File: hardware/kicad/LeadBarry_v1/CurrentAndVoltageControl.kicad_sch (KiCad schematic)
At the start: 37 parts, among them J1 Screw_Terminal_01x02, J2 Screw_Terminal_01x02, J3 Screw_Terminal_01x02, J4 Screw_Terminal_01x02, Q1 SS9014, U2 INA3221_Module, U3 LM2596S_Module

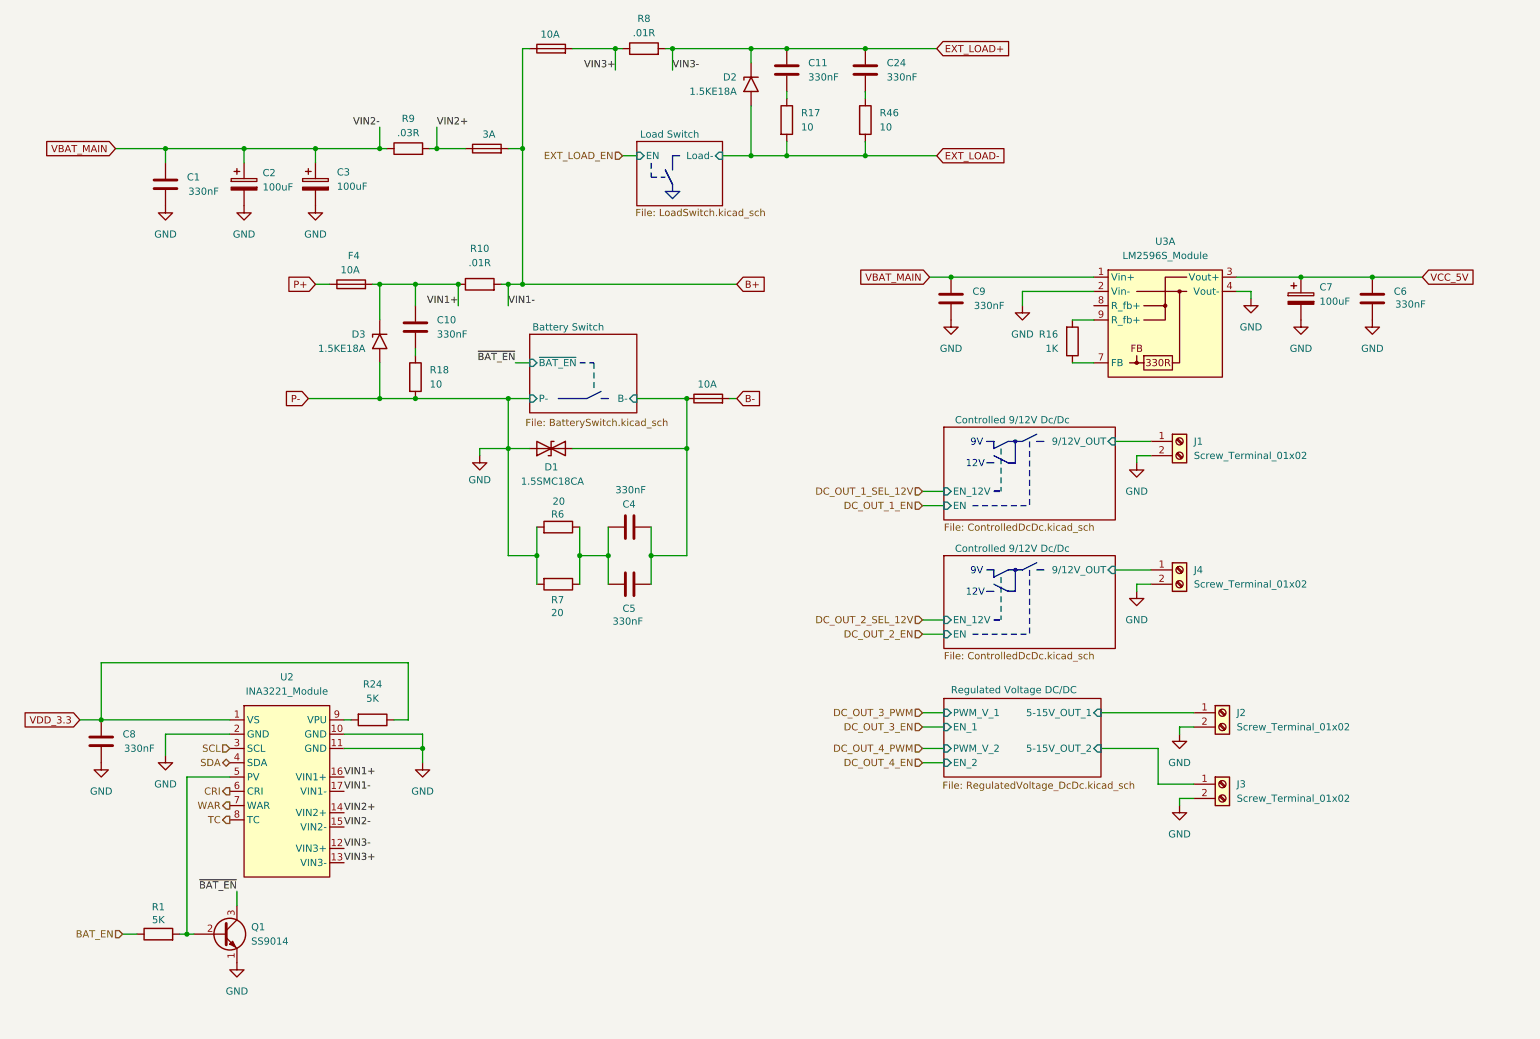
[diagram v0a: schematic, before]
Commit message: fix: PoE sockets and DC output status leds were added
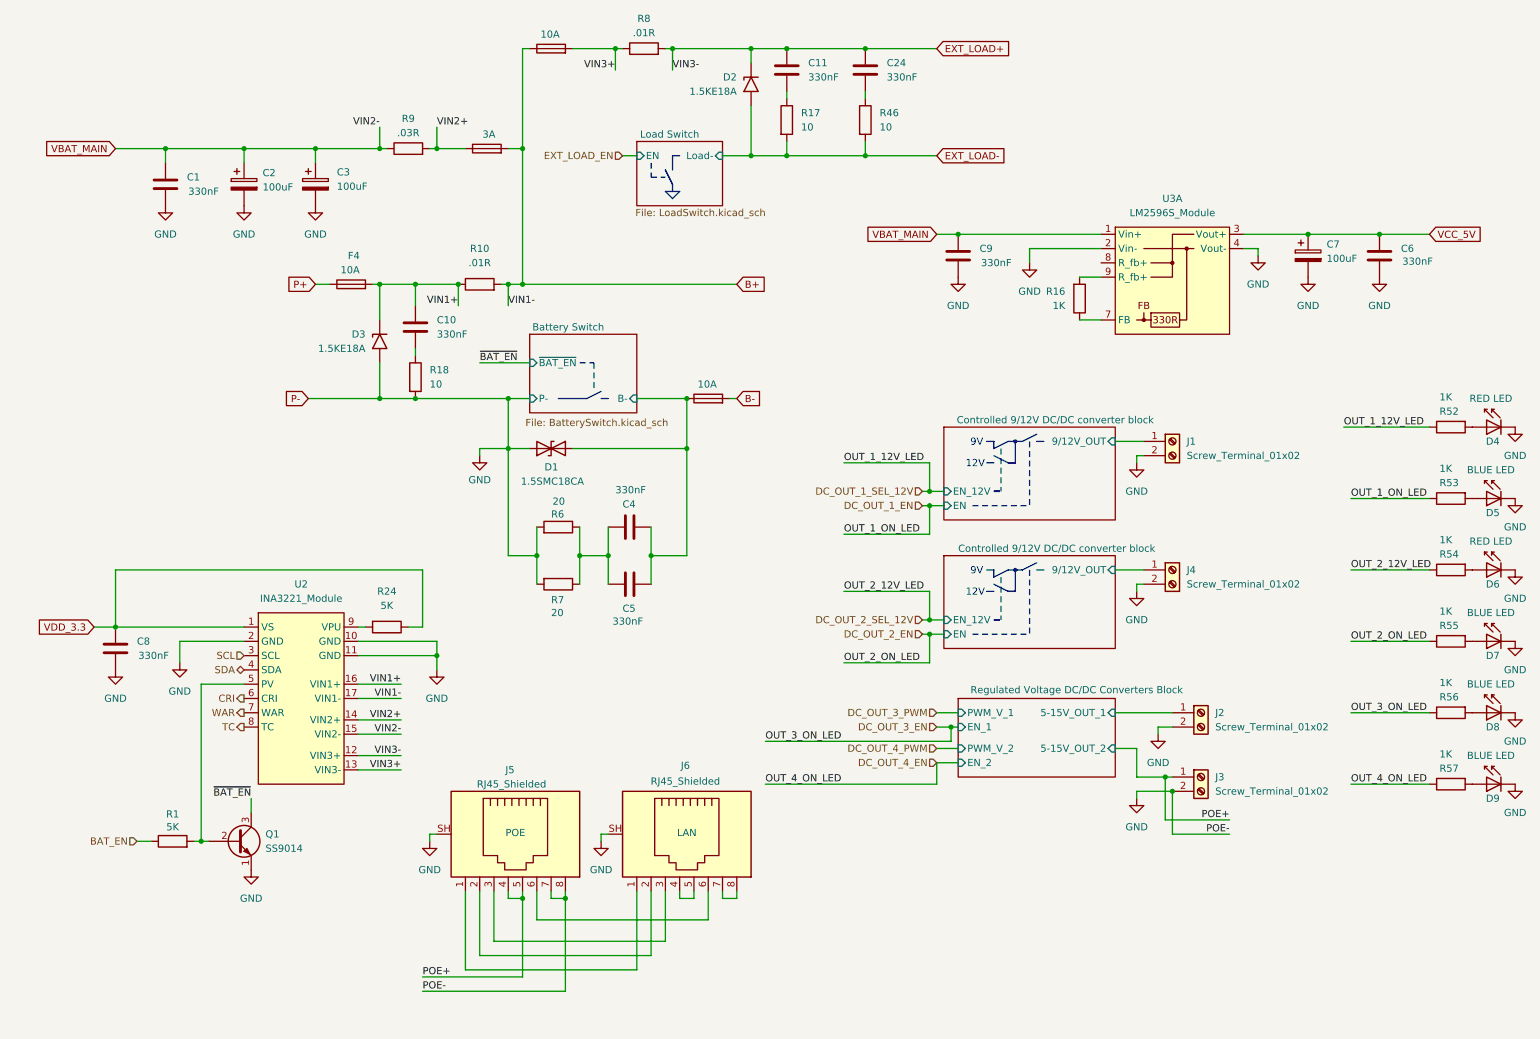
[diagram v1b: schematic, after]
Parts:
- added D4, D5, D6, D7, D8, D9: CQY99, LED_SMD:LED_1206_3216Metric_Pad1.42x1.75mm_HandSolder, symbol LED:CQY99
- added J5, J6: RJ45_Shielded, Connector_RJ:RJ45_Ninigi_GE, symbol Connector:RJ45_Shielded
- added R52, R53, R54, R55, R56, R57: 1K, Resistor_SMD:R_0805_2012Metric_Pad1.20x1.40mm_HandSolder, symbol Device:R
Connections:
- net DC_OUT_1_EN: now also R53.1
- net DC_OUT_1_SEL_12V: now also R52.1
- net DC_OUT_2_EN: now also R55.1
- net DC_OUT_2_SEL_12V: now also R54.1
- net DC_OUT_3_EN: now also R56.1
- net DC_OUT_4_EN: now also R57.1
- net GND: now also D4.1 (K), D5.1 (K), D6.1 (K), D7.1 (K), D8.1 (K), D9.1 (K), J5.7, J5.8, J5.SH, J6.SH
- net Regulated Voltage DC DC/5-15V_OUT_2 renamed POE+
- net POE+: now also J5.4, J5.5
- new net: D4.2 (A), R52.2
- new net: D9.2 (A), R57.2
- new net: D6.2 (A), R54.2
- new net: J5.1, J6.1
- new net: J5.2, J6.2
- new net: J5.3, J6.3
- new net: J6.4, J6.5
- new net: J5.6, J6.6
- new net: J6.7, J6.8
- new net: D8.2 (A), R56.2
- new net: D7.2 (A), R55.2
- new net: D5.2 (A), R53.2
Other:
- title: (none) -> Power management block
- moved on the sheet: C6, C7, C8, C9, J1, J2, J3, J4, Q1, R1, R16, R24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

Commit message: fix: schematic improvement
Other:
- title: Power management block -> Power Management Block
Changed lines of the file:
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@@
 	(paper "A4")
 	(title_block
-		(title "Power management block")
+		(title "Power Management Block")
 		(date "2026-03-21")
 	)

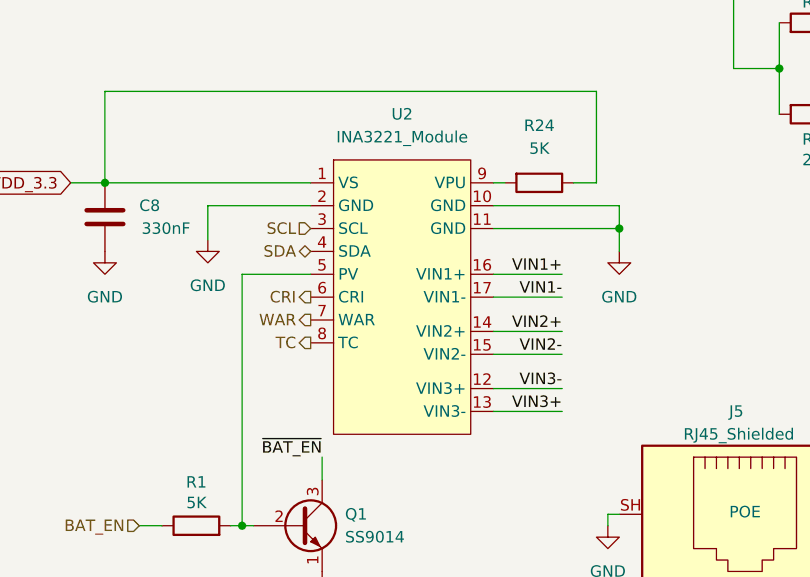
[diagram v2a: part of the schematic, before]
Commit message: fix: added display and timer to the schematic
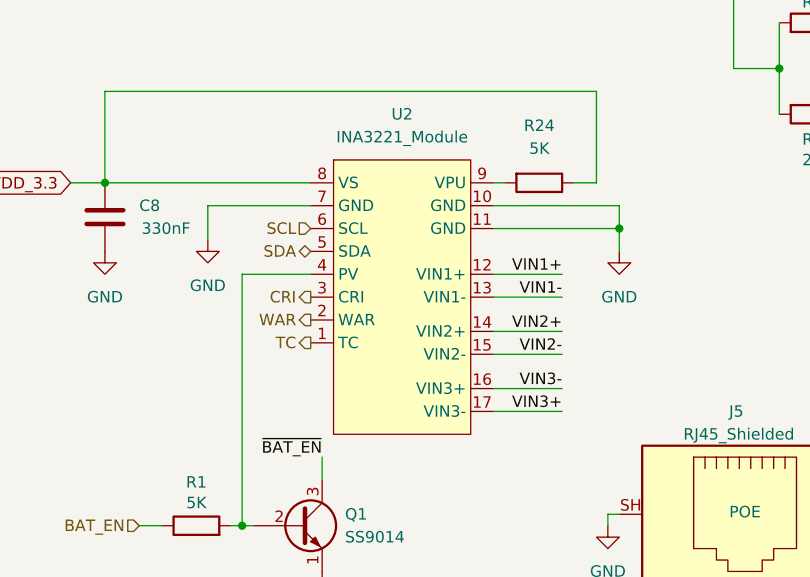
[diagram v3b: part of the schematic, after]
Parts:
- U2: footprint (none) -> Module:INA3221_Mpdule
- U3: footprint Module:LM2596S_Module -> Module:LM2596S_ModuleSide
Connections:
- net B+: now also U2.13 (VIN1-); no longer U2.17 (VIN1-)
- net CRI: now also U2.3 (CRI); no longer U2.6 (CRI)
- net EXT_LOAD+: now also U2.16 (VIN3+); no longer U2.12 (VIN3+)
- net GND: now also U2.7 (GND); no longer U2.2 (GND)
- net SCL: now also U2.6 (SCL); no longer U2.3 (SCL)
- net SDA: now also U2.5 (SDA); no longer U2.4 (SDA)
- net TC: now also U2.1 (TC); no longer U2.8 (TC)
- net VDD_3.3: now also U2.8 (VS); no longer U2.1 (VS)
- net VIN1+: now also U2.12 (VIN1+); no longer U2.16 (VIN1+)
- net VIN3+: now also U2.17 (VIN3-); no longer U2.13 (VIN3-)
- net WAR: now also U2.2 (WAR); no longer U2.7 (WAR)
- net at Q1.2 (B), R1.2: now also U2.4 (PV); no longer U2.5 (PV)
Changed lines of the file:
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@@
 	(wire
 		(pts
-			(xy 232.41 58.42) (xy 234.95 58.42)
-		)
-		(stroke
-			(width 0)
-			(type default)
-		)
-	)
-	(wire
-		(pts
 			(xy 43.18 132.08) (xy 43.18 128.27)
 		)
@@
 	(wire
 		(pts
+			(xy 232.41 58.42) (xy 234.95 58.42)
+		)
+		(stroke
+			(width 0)
+			(type default)
+		)
+	)
+	(wire
+		(pts
 			(xy 31.75 115.57) (xy 31.75 125.73)
 		)
@@
 			)
 		)
-		(property "Footprint" "Module:LM2596S_Module"
+		(property "Footprint" "Module:LM2596S_ModuleSide"
 			(at 219.71 74.93 0)
 			(effects
@@
 			)
 		)
-		(property "Footprint" ""
+		(property "Footprint" "Module:INA3221_Mpdule"
 			(at 66.04 154.94 0)
 			(effects

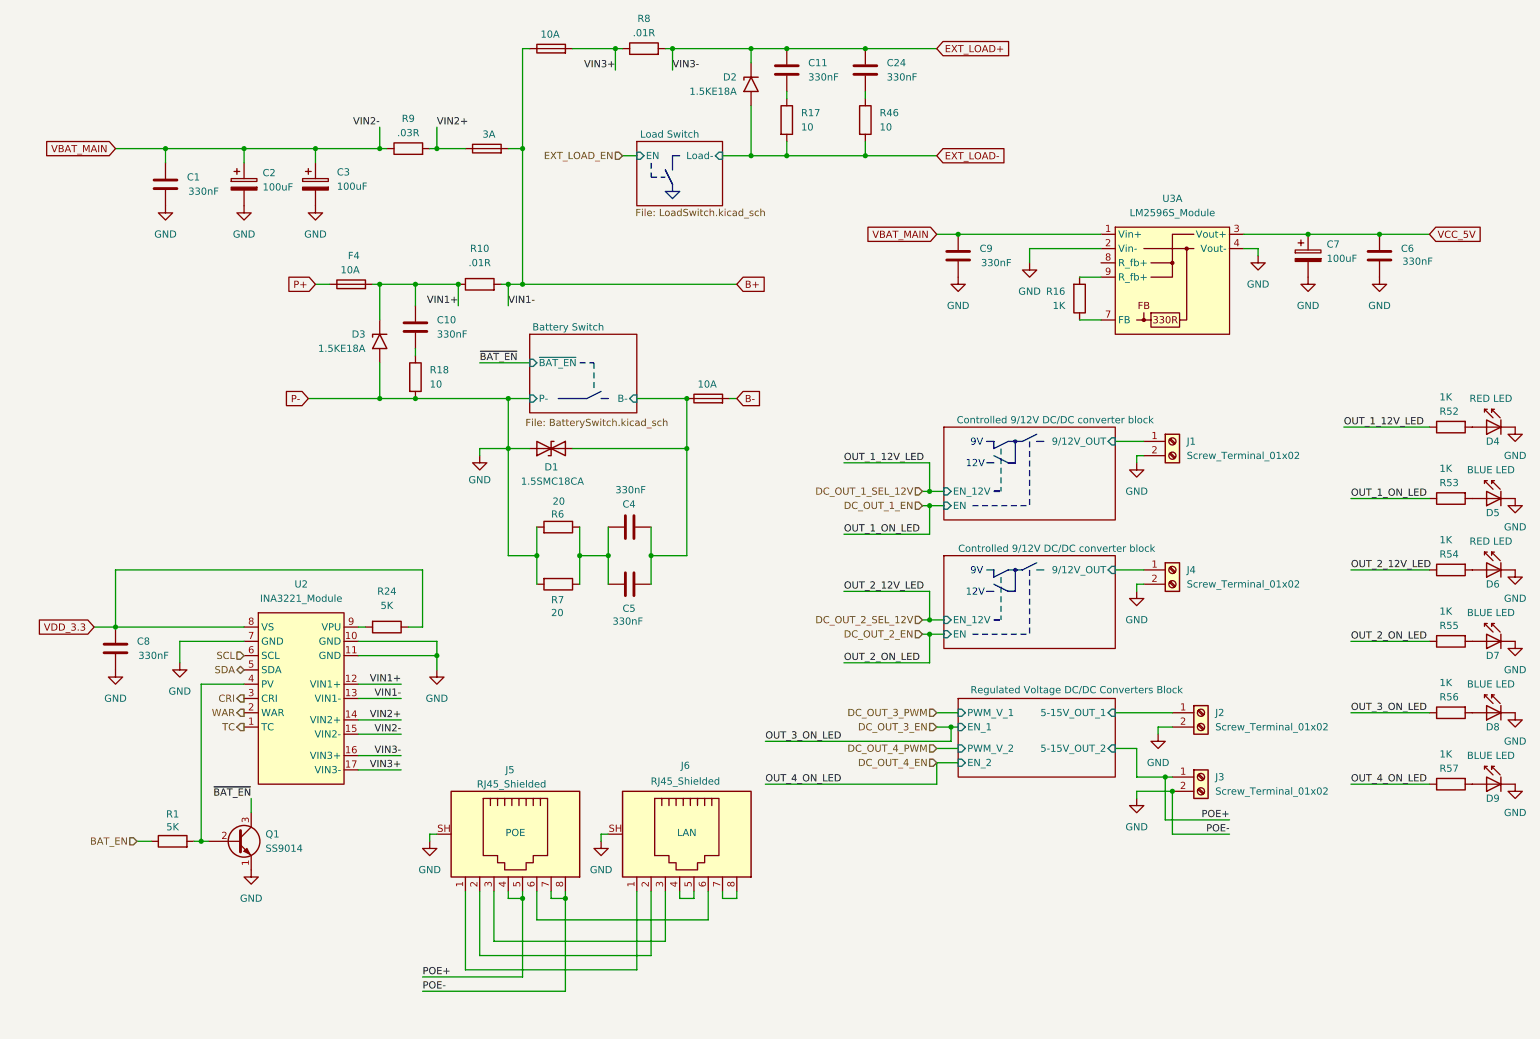
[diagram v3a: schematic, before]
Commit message: fix: RS485 port schematic implemented. Added shift+latch register as a port extension to control the DC outputs.
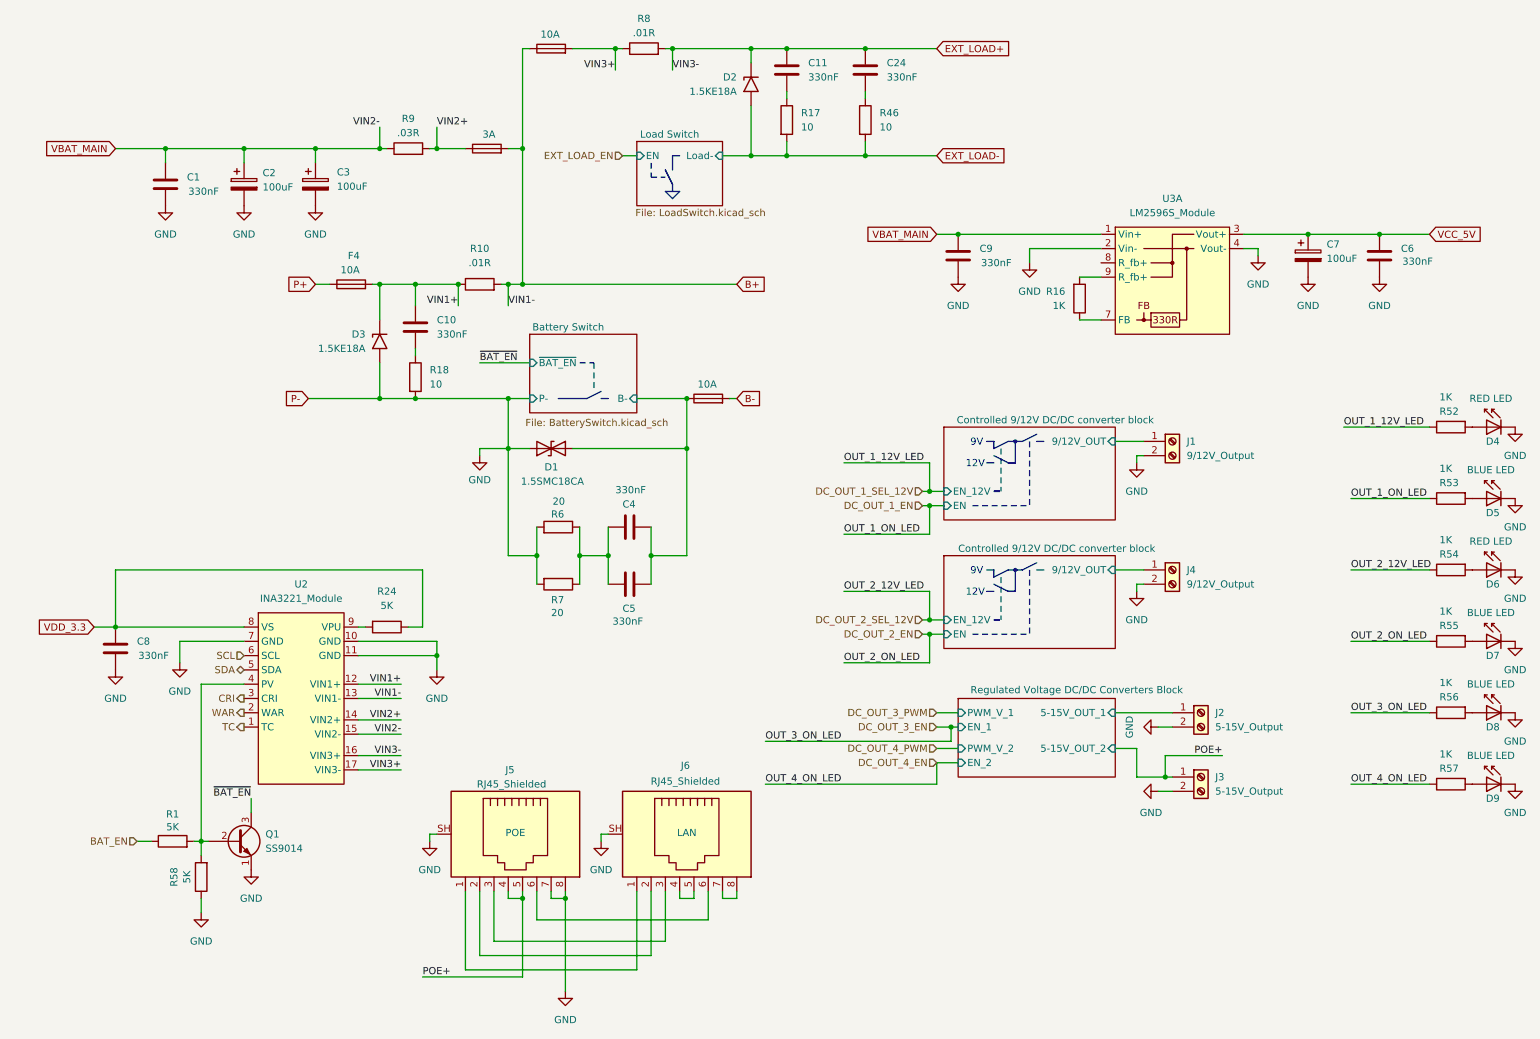
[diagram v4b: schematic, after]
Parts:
- added R58: 5K, Resistor_THT:R_Axial_DIN0207_L6.3mm_D2.5mm_P10.16mm_Horizontal, symbol Device:R
- J1, J4: value Screw_Terminal_01x02 -> 9/12V_Output
- J2, J3: value Screw_Terminal_01x02 -> 5-15V_Output
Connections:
- net GND: now also R58.1
- net at Q1.2 (B), R1.2, U2.4 (PV): now also R58.2
